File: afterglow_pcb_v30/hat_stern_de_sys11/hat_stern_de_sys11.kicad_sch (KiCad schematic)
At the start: 8 parts, among them J1 ROW OUT, J2 COLUMN OUT, J3 Conn_01x09_Pin, J4 Conn_01x10_Pin, J5 Conn_01x10_Pin, J6 Conn_01x09_Pin, J7 Conn_02x03_Odd_Even, J8 Conn_02x03_Odd_Even

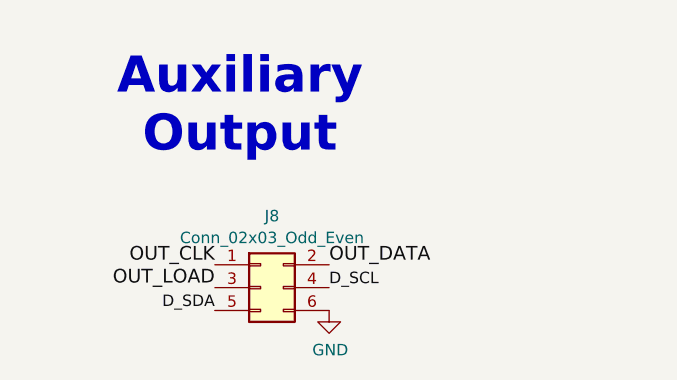
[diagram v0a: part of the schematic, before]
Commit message: Pinbender hat v1.1. Fixes a short of the I2C to ground.
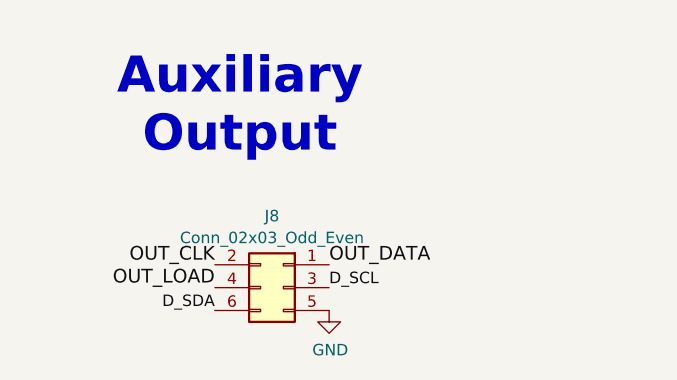
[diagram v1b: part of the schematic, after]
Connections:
- net D_SCL: now also J8.3 (Pin_3); no longer J8.4 (Pin_4)
- net D_SDA: now also J8.6 (Pin_6); no longer J8.5 (Pin_5)
- net GND: now also J8.5 (Pin_5); no longer J8.6 (Pin_6)
- net OUT_CLK: now also J8.2 (Pin_2); no longer J8.1 (Pin_1)
- net OUT_DATA: now also J8.1 (Pin_1); no longer J8.2 (Pin_2)
- net OUT_LOAD: now also J8.4 (Pin_4); no longer J8.3 (Pin_3)
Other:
- title: Afterglow 3.0 Hat -> Afterglow 3.0 Pinbender Hat
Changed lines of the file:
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@@
 	(paper "A4")
 	(title_block
-		(title "Afterglow 3.0 Hat")
-		(rev "1.0")
+		(title "Afterglow 3.0 Pinbender Hat")
+		(rev "1.1")
 		(company "bitfield labs")
 	)
@@
 	(symbol
 		(lib_id "Connector_Generic:Conn_02x03_Odd_Even")
-		(at 52.705 164.465 0)
+		(at 55.245 164.465 0)
+		(mirror y)
 		(unit 1)
 		(exclude_from_sim no)
@@
 		)
 		(property "Footprint" "Connector_PinHeader_2.54mm:PinHeader_2x03_P2.54mm_Vertical"
-			(at 52.705 164.465 0)
+			(at 55.245 164.465 0)
 			(effects
 				(font
@@
 		)
 		(property "Datasheet" "~"
-			(at 52.705 164.465 0)
+			(at 55.245 164.465 0)
 			(effects
 				(font
@@
 		)
 		(property "Description" ""
-			(at 52.705 164.465 0)
+			(at 55.245 164.465 0)
 			(effects
 				(font
@@
 		)
 		(property "JLCPCB" "C92272"
-			(at 52.705 164.465 0)
-			(effects
-				(font
+			(at 55.245 164.465 0)
+			(effects
+				(font

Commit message: Improved production files
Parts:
- J1: JLCPCB (none) -> C10589
- J2: JLCPCB (none) -> C10587
- J3, J6: JLCPCB (none) -> C10586
- J4, J5: JLCPCB (none) -> C5156617
- J7, J8: JLCPCB C92272 -> C18905882
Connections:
- net 3V3: now also J7.5 (Pin_5), J7.6 (Pin_6); no longer J7.1 (Pin_1), J7.2 (Pin_2)
- net D_SDA: now also J8.2 (Pin_2); no longer J8.6 (Pin_6)
- net GND: now also J7.1 (Pin_1), J7.2 (Pin_2), J8.1 (Pin_1); no longer J7.5 (Pin_5), J7.6 (Pin_6), J8.5 (Pin_5)
- net OUT_CLK: now also J8.6 (Pin_6); no longer J8.2 (Pin_2)
- net OUT_DATA: now also J8.5 (Pin_5); no longer J8.1 (Pin_1)
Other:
- moved on the sheet: J8
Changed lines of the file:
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@@
+			)
+		)
+		(property "JLCPCB" "C5156617"
+			(at 43.18 64.135 0)
+			(effects
+				(font
+					(size 1.524 1.524)
+				)
+				(hide yes)
 			)
 		)
@@
 			)
 		)
+		(property "JLCPCB" "C10587"
+			(at 137.16 57.785 0)
+			(effects
+				(font
+					(size 1.524 1.524)
+				)
+				(hide yes)
+			)
+		)
 		(pin "1"
 		)
@@
 	(symbol
 		(lib_id "Connector_Generic:Conn_02x03_Odd_Even")
-		(at 55.245 164.465 0)
-		(mirror y)
-		(unit 1)
-		(exclude_from_sim no)
-		(in_bom yes)
-		(on_board yes)
-		(dnp no)
-		(fields_autoplaced yes)
+		(at 55.245 164.465 180)
+		(unit 1)
+		(exclude_from_sim no)
+		(in_bom yes)
+		(on_board yes)
+		(dnp no)
 		(property "Reference" "J8"
-			(at 53.975 156.5107 0)
+			(at 53.975 172.4193 0)
 			(effects
 				(font
@@
 		)
 		(property "Value" "Conn_02x03_Odd_Even"
-			(at 53.975 158.9349 0)
+			(at 53.975 169.9951 0)
 			(effects
 				(font
@@
 			)
 		)
-		(property "JLCPCB" "C92272"
+		(property "JLCPCB" "C18905882"
 			(at 55.245 164.465 0)
 			(effects
@@
 			)
 		)
+		(property "JLCPCB" "C5156617"
+			(at 61.595 60.96 0)
+			(effects
+				(font
+					(size 1.524 1.524)
+				)
+				(hide yes)
+			)
+		)
 		(pin "6"
 		)
@@
 			)
 		)
+		(property "JLCPCB" "C10589"
+			(at 125.095 107.95 0)
+			(effects
+				(font
+					(size 1.524 1.524)
+				)
+				(hide yes)
+			)
+		)
 		(pin "1"
 		)
@@
 		(lib_id "Connector_Generic:Conn_02x03_Odd_Even")
 		(at 47.625 113.665 0)
-		(unit 1)
-		(exclude_from_sim no)
-		(in_bom yes)
-		(on_board yes)
-		(dnp no)
-		(fields_autoplaced yes)
+		(mirror x)
+		(unit 1)
+		(exclude_from_sim no)
+		(in_bom yes)
+		(on_board yes)
+		(dnp no)
 		(property "Reference" "J7"
-			(at 48.895 105.7107 0)
+			(at 48.895 121.6193 0)
 			(effects
 				(font
@@
 		)
 		(property "Value" "Conn_02x03_Odd_Even"
-			(at 48.895 108.1349 0)
+			(at 48.895 119.1951 0)
 			(effects
 				(font
@@
 			)
 		)
-		(property "JLCPCB" "C92272"
+		(property "JLCPCB" "C18905882"
 			(at 47.625 113.665 0)
 			(effects
@@
 			)
 		)
+		(property "JLCPCB" "C10586"
+			(at 192.405 58.42 0)
+			(effects
+				(font
+					(size 1.524 1.524)
+				)
+				(hide yes)
+			)
+		)
 		(pin "6"
 		)
@@
 				)
 				(hide yes)
+			)
+		)
+		(property "JLCPCB" "C10586"
+			(at 177.8 106.045 0)
+			(effects
+				(font
+					(size 1.524 1.524)
+				)
+				(hide yes)
